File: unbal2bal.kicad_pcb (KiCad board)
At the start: 2 copper layers, 76 x 90 mm, 36 parts, among them J1 RCJ-041, J2 NRJ3HF-1, J3 Mini-DIN-3, J4 Mini-DIN-4, U1 LM4562

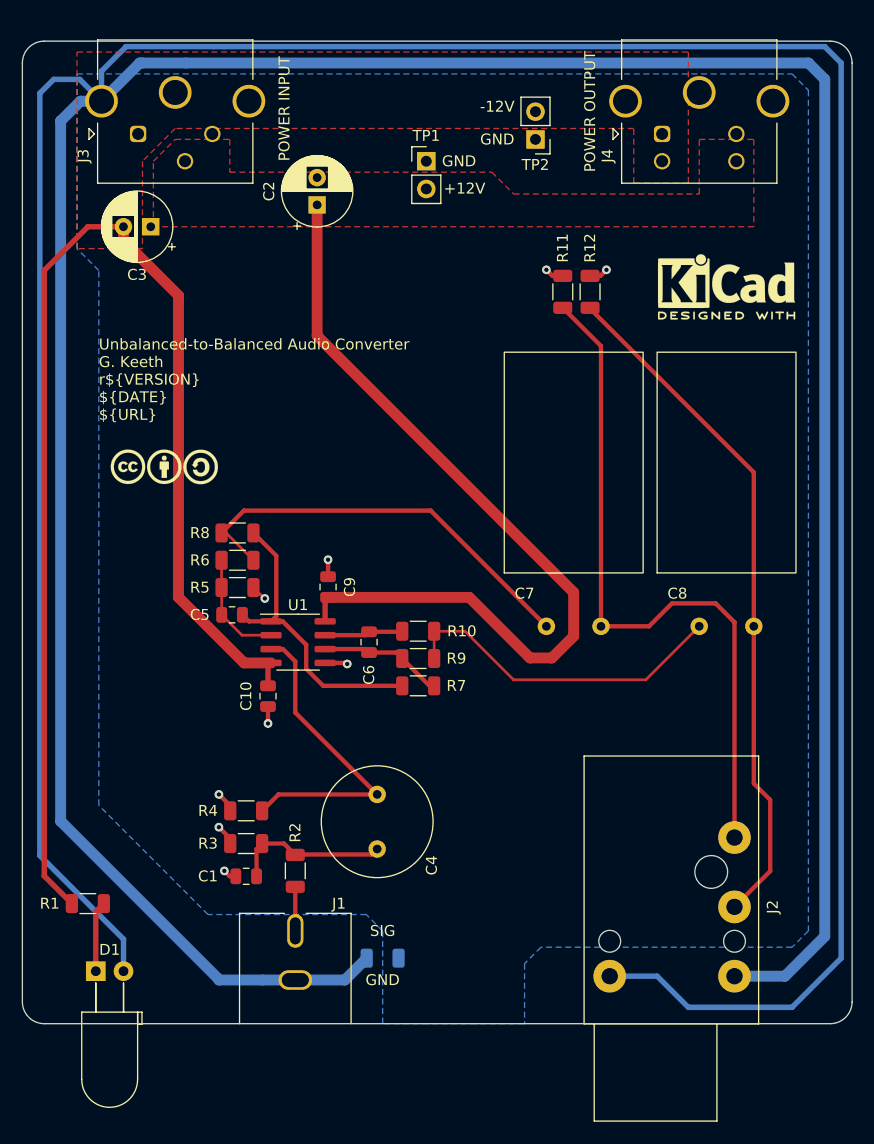
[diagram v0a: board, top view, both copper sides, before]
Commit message: Adjust DIN connector locations
- move miniDIN (power) connectors backwards 1.6mm to be flush with
  outside of case for connector clearance
- not going to increase size of cutouts for miniDIN connectors in back
  panel. Moving the connectors fixes the connector clearance issue, and
  existing cutouts have a minimal amount of slop so hopefully that
  should be enough for assembly tolerances.
- rework star grounding as a result of moving power connectors
- increase annular ring size on miniDIN connector footprints
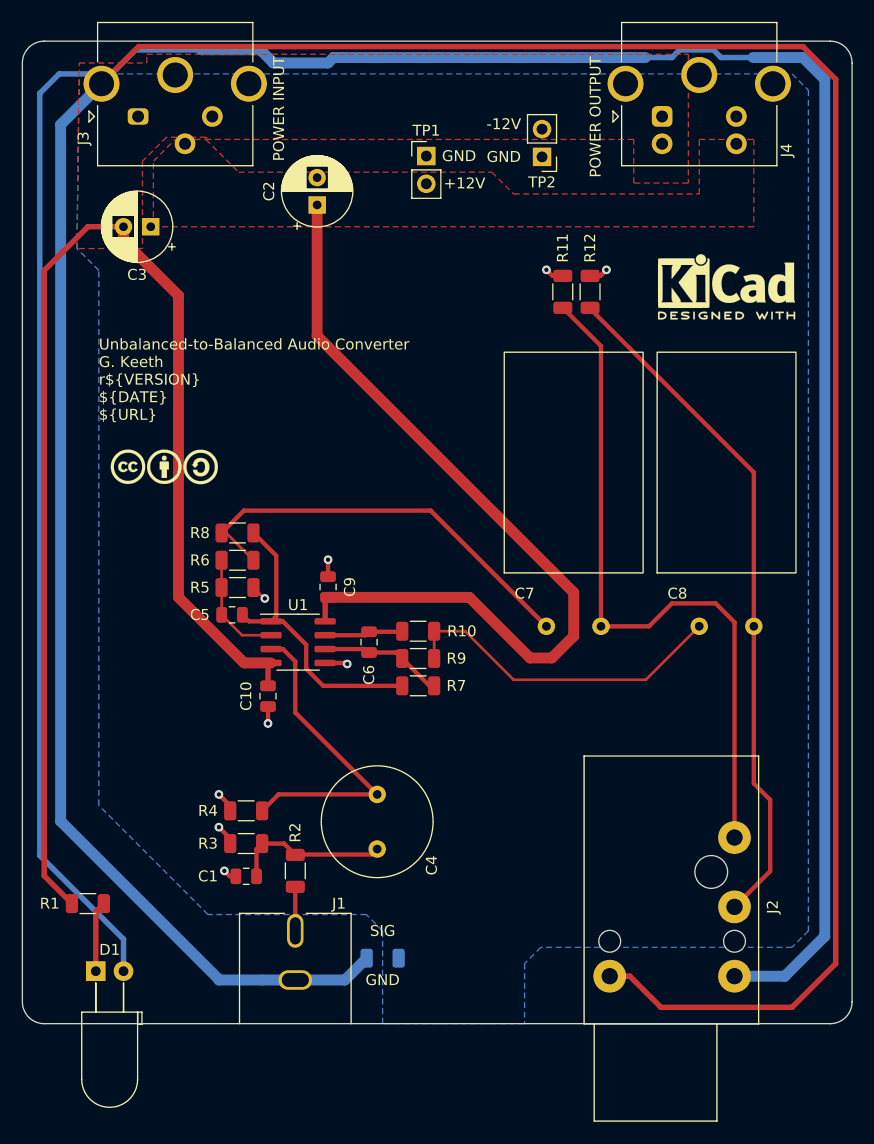
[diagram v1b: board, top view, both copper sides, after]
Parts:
- NT3: moved to F.Cu
- moved NT2 13.0 mm to (126.0, 62.0)
- moved NT3 6.50 mm to (124.5, 60.5)
- moved TP2 1.71 mm to (147.6, 70.6)
- moved J3 1.60 mm to (110.6, 66.9)
- moved J4 1.60 mm to (158.6, 66.9)
- moved TP1 0.47 mm to (137.0, 70.5)
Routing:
- net GND: track 214.1 -> 231.9 mm
- net Net-(J2-PadS): track 147.4 -> 135.4 mm
- net Net-(J2-PadG): track 163.4 -> 155.3 mm

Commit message: add mask cutout for balanced jack panel grounding
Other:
- board text added: "TODO 3d model for NRJ3HF-1"
- board text removed: "TODO 3d model for NRJ3HF-1 add front panel grounding ring to 1/4{dblquote} jack front panel? Double check horizontal position of 1/4{dblquote} jack"
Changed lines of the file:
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@@
     (effects (font (size 1 1) (thickness 0.15)) (justify left))
   )
-  (gr_text "TODO\n\n3d model for NRJ3HF-1\nadd front panel grounding ring to 1/4{dblquote} jack front panel?\nDouble check horizontal position of 1/4{dblquote} jack" (at 226.5 91.5) (layer "Cmts.User")
+  (gr_text "TODO\n\n3d model for NRJ3HF-1" (at 226.5 91.5) (layer "Cmts.User")
     (effects (font (size 1.5 1.5) (thickness 0.3)) (justify left))
   )

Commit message: add 3D model for output jack, update date
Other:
- board text removed: "TODO 3d model for NRJ3HF-1"
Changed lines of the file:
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@@
     )
   )
-  (property "DATE" "2022-07-04")
+  (property "DATE" "2022-08-28")
   (property "URL" "github.com/gkeeth/unbal2bal")
   (property "VERSION" "1")
@@
       (rotate (xyz 0 0 0))
     )
+    (model "${KICAD6_USER_3DMODEL_DIR}/Connector_Audio_gkeeth.3dshapes/Jack_6.35mm_Neutrik_NRJ3HF-1_Horizontal.wrl"
+      (offset (xyz 0 0 0))
+      (scale (xyz 1 1 1))
+      (rotate (xyz 0 0 0))
+    )
   )
   (footprint "Symbol:KiCad-Logo2_5mm_SilkScreen" (layer "F.Cu")
@@
     (effects (font (size 1 1) (thickness 0.15)) (justify left))
   )
-  (gr_text "TODO\n\n3d model for NRJ3HF-1" (at 226.5 91.5) (layer "Cmts.User")
-    (effects (font (size 1.5 1.5) (thickness 0.3)) (justify left))
-  )
   (dimension (type aligned) (layer "Dwgs.User")
